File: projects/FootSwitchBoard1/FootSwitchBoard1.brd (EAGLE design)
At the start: 50 x 50 mm, 46 parts

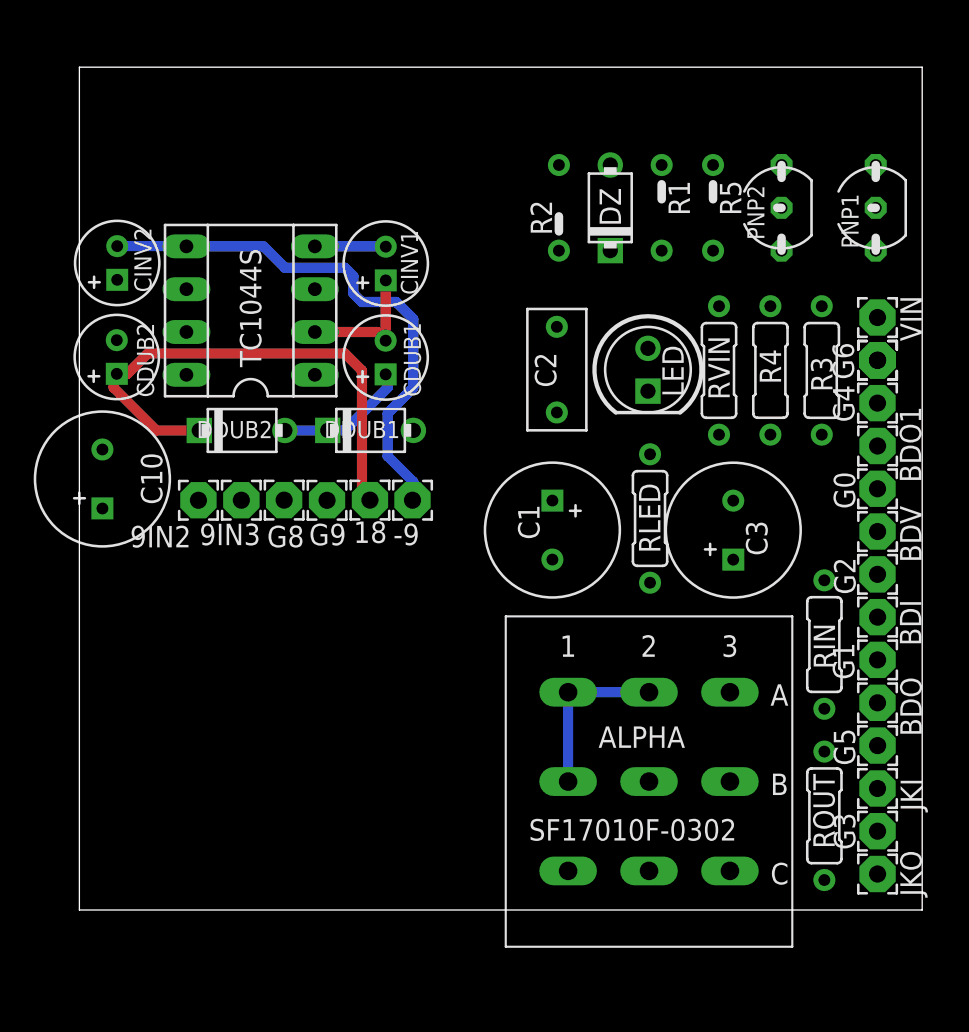
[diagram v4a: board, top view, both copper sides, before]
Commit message: Work in progress, switching back to reverse polarity protection only.
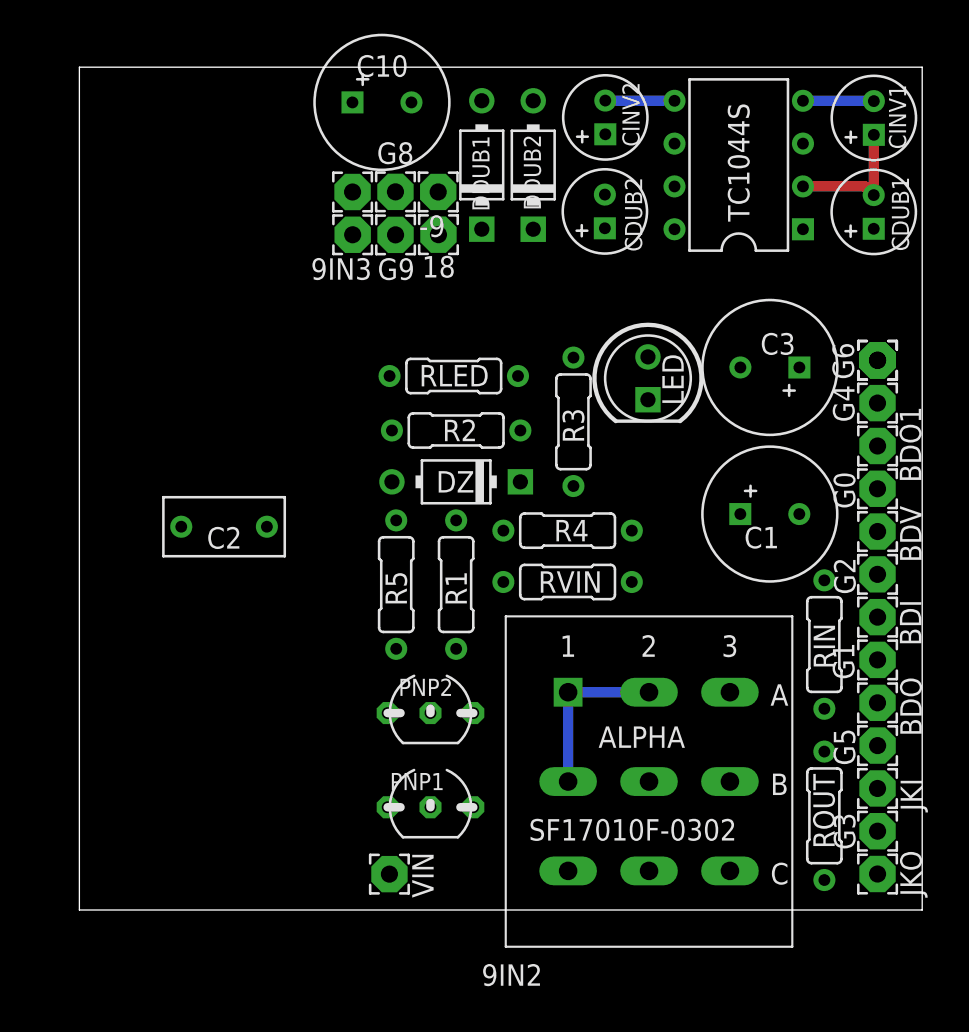
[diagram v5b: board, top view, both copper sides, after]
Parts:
- DDUB1, DDUB2: value 1N58172 -> (none); device gm-diodes:DO41-2 -> gm-diodes:DO41-3
- DZ: device gm-diodes:DO41-2 -> gm-diodes:DO41-3
- R1, R2, R5: device gm-resistors:R0207/2V -> gm-resistors:R0207/3
- TC1044S: device ic-package:SOCKET-08 -> gm-ics:DIL08
- moved PNP1 44.3 mm to (20.8, 6.10), turned to 0 degrees
- moved VIN 43.9 mm to (18.4, 2.13)
- moved PNP2 36.5 mm to (20.8, 11.7), turned to 0 degrees
- moved CDUB2 30.2 mm to (31.2, 41.4)
- moved CINV1 30.2 mm to (47.1, 47.0)
- moved CDUB1 30.2 mm to (47.1, 41.4)
- moved CINV2 30.2 mm to (31.2, 47.0)
- moved TC1044S 30.2 mm to (39.1, 44.2)
- moved R5 29.2 mm to (18.8, 19.3), turned to 90 degrees
- moved C10 27.8 mm to (17.9, 47.9), turned to 0 degrees
- moved R1 25.5 mm to (22.4, 19.3), turned to 90 degrees
- moved DDUB2 23.4 mm to (26.9, 44.2), turned to 90 degrees
- moved C2 21.8 mm to (8.58, 22.7), turned to 180 degrees
- moved 9IN2 20.4 mm to (16.2, 42.6)
- moved G8 19.4 mm to (18.8, 42.6)
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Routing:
- net N$22: track 30.4 -> 0.00 mm
- net N$19: track 32.0 -> 4.11 mm
- net DDUB2: track 7.99 -> 0.00 mm

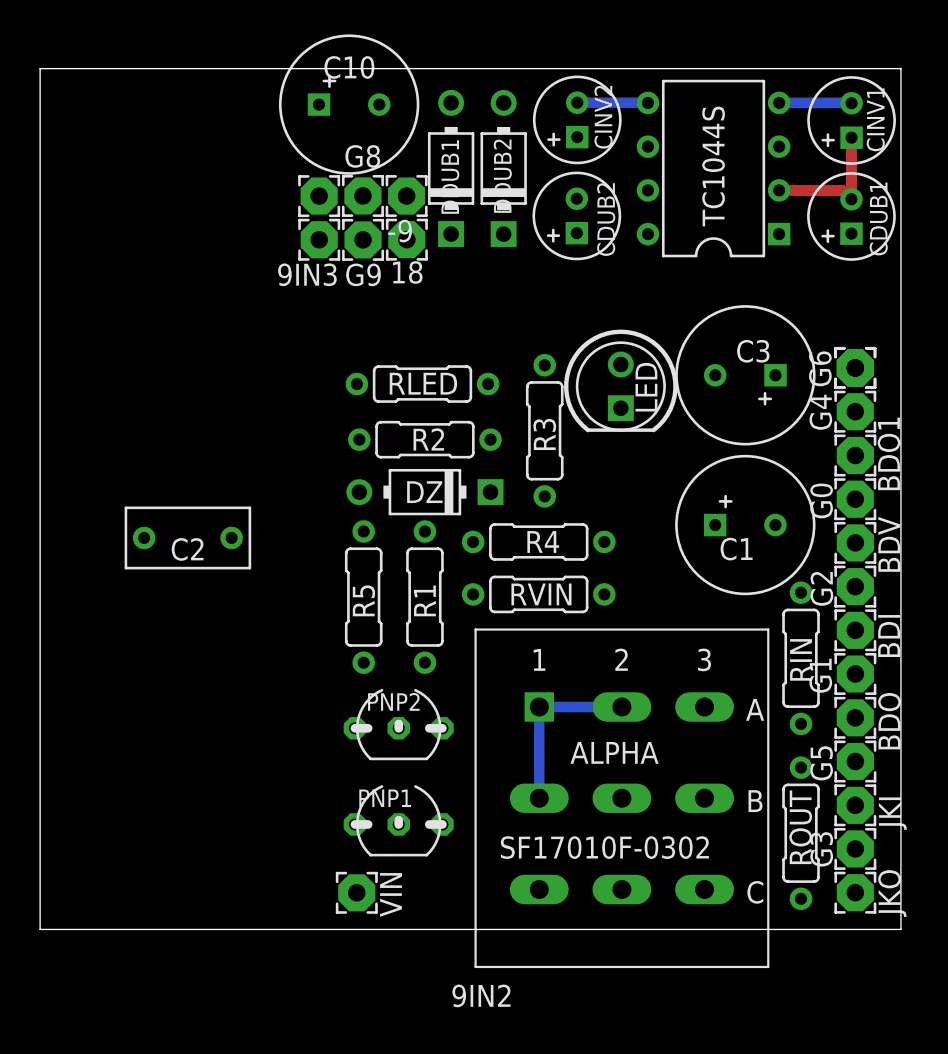
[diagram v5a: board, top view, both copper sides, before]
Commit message: Good layout with reverse polarity protection.
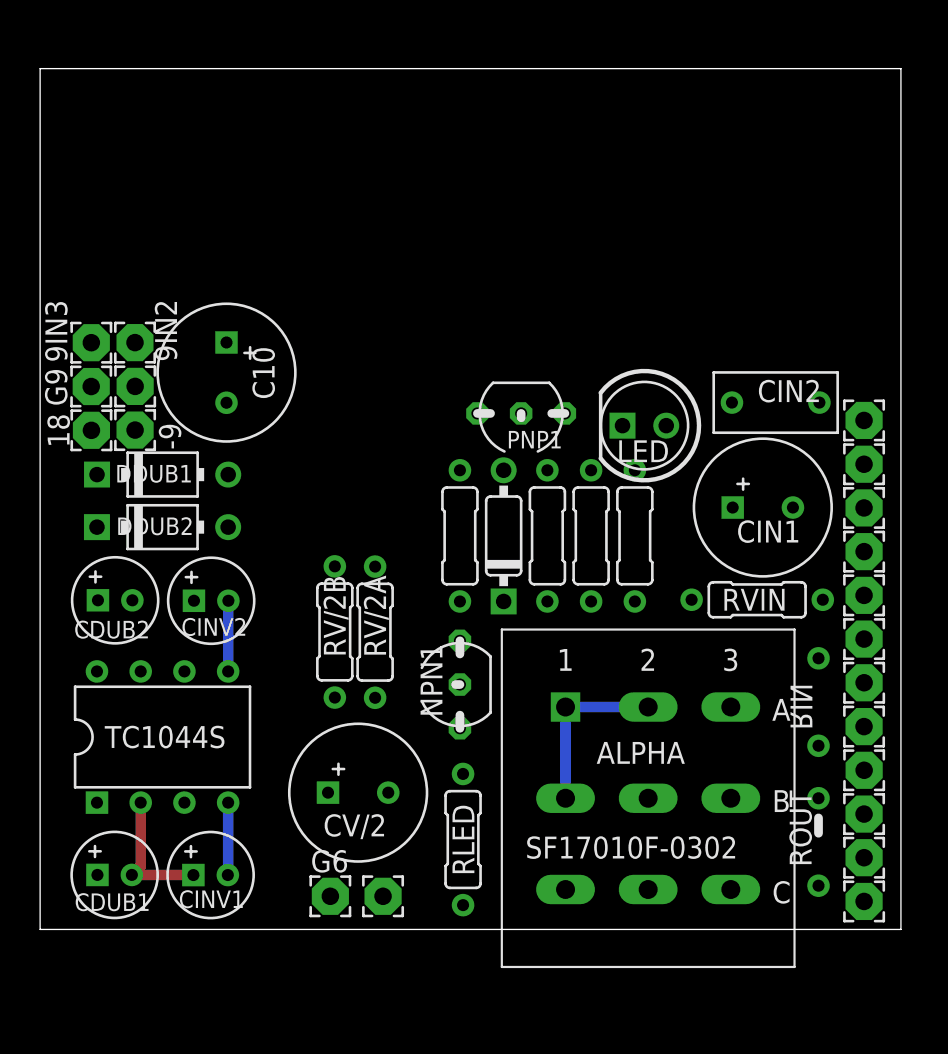
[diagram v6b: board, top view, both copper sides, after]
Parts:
- removed BDO1: WIREPAD2,15/1,0, wirepad:2,15/1,0
- removed C1, C3: 100u, gm-caps-electro-pol:080_035
- removed C2: 100n, gm-caps-film-box:072X035
- removed DZ: (no value), gm-diodes:DO41-3
- removed PNP2: 2N3906-, gm-trans:TO92-
- removed R3, R4: (no value), gm-resistors:R0207/3
- added CIN1, CV/2: 100u, gm-caps-electro-pol:080_035
- added CIN2: 100n, gm-caps-film-box:072X035
- added D1: 1N4148-3, gm-diodes:DO35-3
- added NPN1: 2N3904, gm-trans:TO92-
- added R6: 4M7, gm-resistors:R0207/3
- added RV/2A, RV/2B: (no value), gm-resistors:R0207/3
- R1: value 10k -> 100K
- R2: value 10k -> 3K3
- R5: value 100k -> 10K
- RIN, ROUT: device gm-resistors:R0207/3 -> gm-resistors:R0207/2V
- moved CINV1 57.5 mm to (9.90, 3.16), turned to 0 degrees
- moved CDUB1 57.4 mm to (4.33, 3.17), turned to 0 degrees
- moved TC1044S 46.0 mm to (7.11, 11.2), turned to 0 degrees
- moved G6 43.3 mm to (16.9, 1.93), turned to 0 degrees
- moved V/2 41.2 mm to (19.9, 1.93), turned to 270 degrees
- moved VIN 38.6 mm to (47.9, 27.0)
- moved CINV2 35.1 mm to (9.94, 19.1), turned to 0 degrees
- moved CDUB2 34.9 mm to (4.36, 19.1), turned to 0 degrees
- moved DDUB2 28.7 mm to (7.11, 23.4), turned to 0 degrees
- moved RLED 26.6 mm to (24.6, 5.22), turned to 270 degrees
- moved PNP1 24.9 mm to (27.9, 30.0), turned to 180 degrees
- moved DDUB1 24.4 mm to (7.12, 26.4), turned to 0 degrees
- moved 18 21.4 mm to (2.98, 29.0), turned to 0 degrees
- moved -9 20.8 mm to (5.52, 29.0), turned to 90 degrees
- moved G9 17.9 mm to (2.97, 31.5), turned to 90 degrees
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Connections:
- removed net N$23: PNP1.2, PNP2.1, R1.2
- removed net N$3: BDO.1, BDO1.1, U$1.C3
- removed net N$4: BDI.1, U$1.B2
- new net N$11: BDO.1, ROUT.2, U$1.C3
- new net N$7: PNP1.2, R2.2, R6.1
- new net N$8: BDI.1, RIN.2, U$1.B2
- net 9INDUBINV: now also CIN1.+, CIN2.1; no longer C1.+, C2.1
- net GDUBINV: now also CIN1.-, CIN2.2, CV/2.-, D1.A, NPN1.3, RV/2B.1; no longer C1.-, C2.2, C3.-, DZ.A, R4.1
- net N$1: no longer RIN.2
- net N$10: now also CV/2.+, RV/2A.1, RV/2B.2; no longer C3.+, R3.1, R4.2
- net N$14: now also D1.C, NPN1.2, R1.2; no longer DZ.C, R2.1
- net N$2: no longer ROUT.2
- net N$24: now also R6.2; no longer PNP2.3
- net N$25: now also RV/2A.2; no longer R3.2
- net N$9: now also NPN1.1, R2.1; no longer PNP2.2, R2.2
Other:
- board text removed: "INVERTER BD"

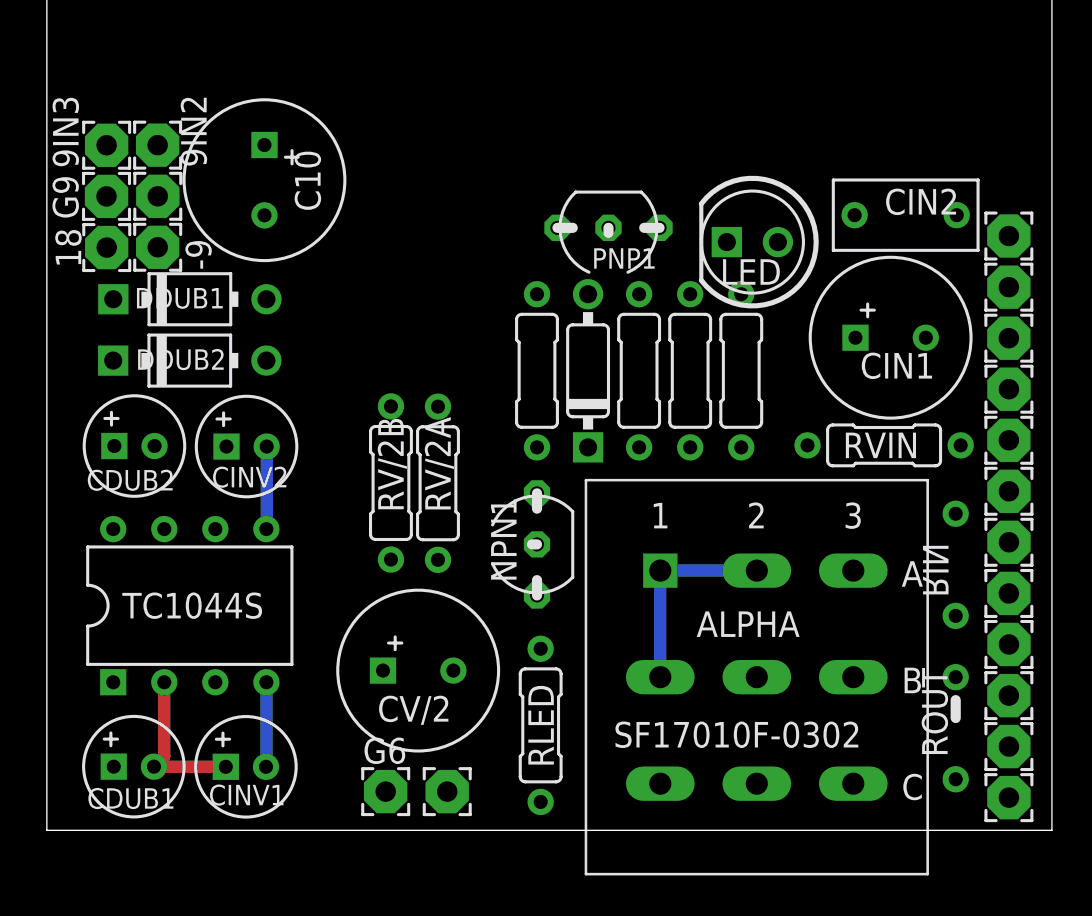
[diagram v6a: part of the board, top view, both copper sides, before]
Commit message: Finalized layout with ground and power planes.
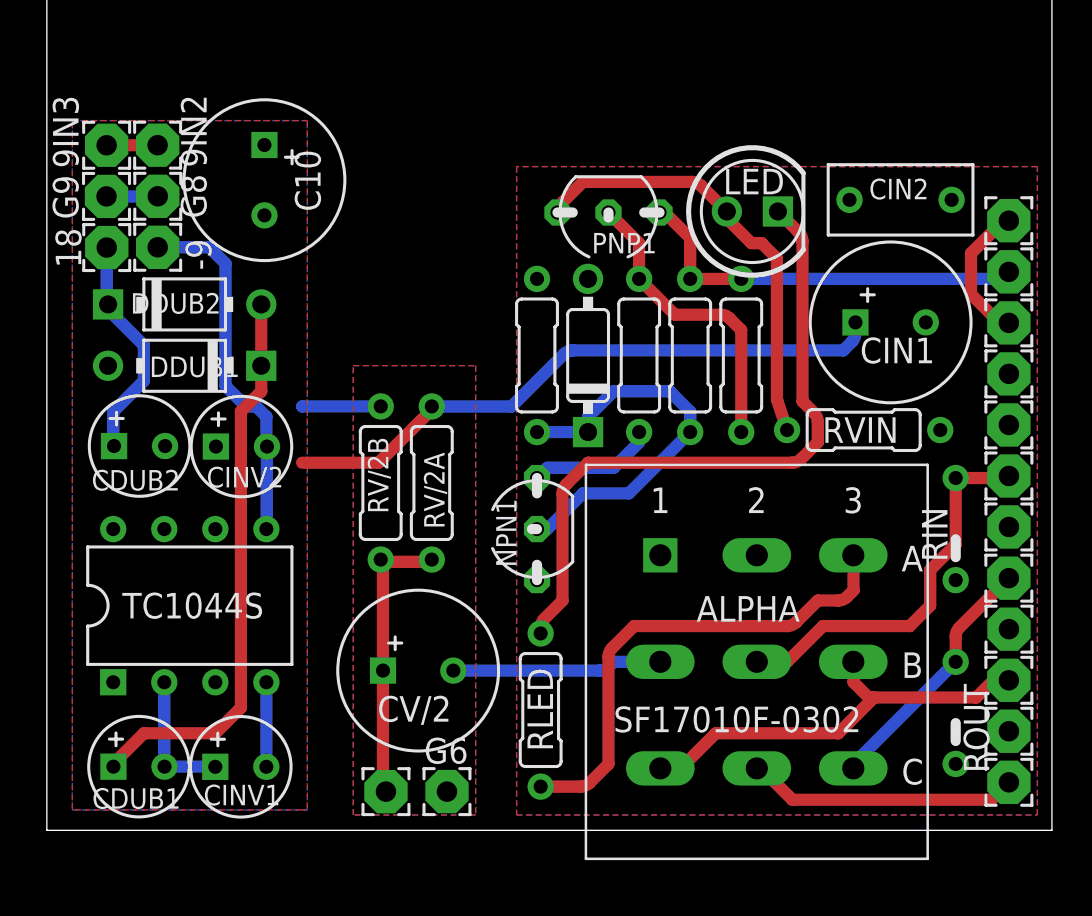
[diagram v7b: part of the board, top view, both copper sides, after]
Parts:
- CDUB1, CDUB2, CINV1, CINV2: device gm-caps-electro-pol:050_020 -> gm-caps-electro-pol:050_020_1
- moved DDUB1 3.32 mm to (6.85, 23.1), turned to 180 degrees
- moved G6 3.05 mm to (19.9, 1.93)
- moved V/2 3.05 mm to (16.9, 1.93)
- moved DDUB2 2.81 mm to (6.86, 26.2)
- moved RIN 1.78 mm to (45.2, 15.0), flipped to the top
- moved LED 1.52 mm to (35.1, 30.8), turned to 0 degrees
- moved RVIN 1.27 mm to (40.6, 19.9)
- moved CIN2 0.80 mm to (42.5, 31.4)
- moved BDO 0.76 mm to (47.9, 12.5)
- moved BDV 0.76 mm to (47.9, 22.7)
- moved CIN1 0.76 mm to (42.0, 25.3)
- moved D1 0.76 mm to (26.9, 23.6)
- moved G0 0.76 mm to (47.9, 25.2)
- moved G1 0.76 mm to (47.9, 15.1)
- moved G2 0.76 mm to (47.9, 20.2)
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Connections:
- removed net N$25: LED.A, PNP1.1, RV/2A.2, RVIN.1
- new net N$4: LED.A, PNP1.1, RVIN.1
- net 9INDUBINV: now also RV/2A.2
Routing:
- net 9INDUBINV: track 0.00 -> 33.4 mm
- net N$5: track 0.00 -> 33.4 mm
- net DDUB2: track 0.00 -> 28.1 mm
- net N$6: track 0.00 -> 24.5 mm
- net N$4: track 0.00 -> 22.0 mm
- net N$1: track 0.00 -> 21.5 mm
- net N$24: track 0.00 -> 20.0 mm
- net N$14: track 0.00 -> 20.0 mm
- net N$8: track 0.00 -> 19.3 mm
- net N$7: track 0.00 -> 15.1 mm
- net N$10: track 0.00 -> 14.1 mm
- net N$19: track 4.11 -> 18.1 mm
- net GDUBINV: track 10.1 -> 24.0 mm
- net N$2: track 0.00 -> 13.5 mm
- net N$11: track 0.00 -> 12.6 mm
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- added copper zone on layer 1, net 9INDUBINV
- added copper zone on layer 16, net GDUBINV

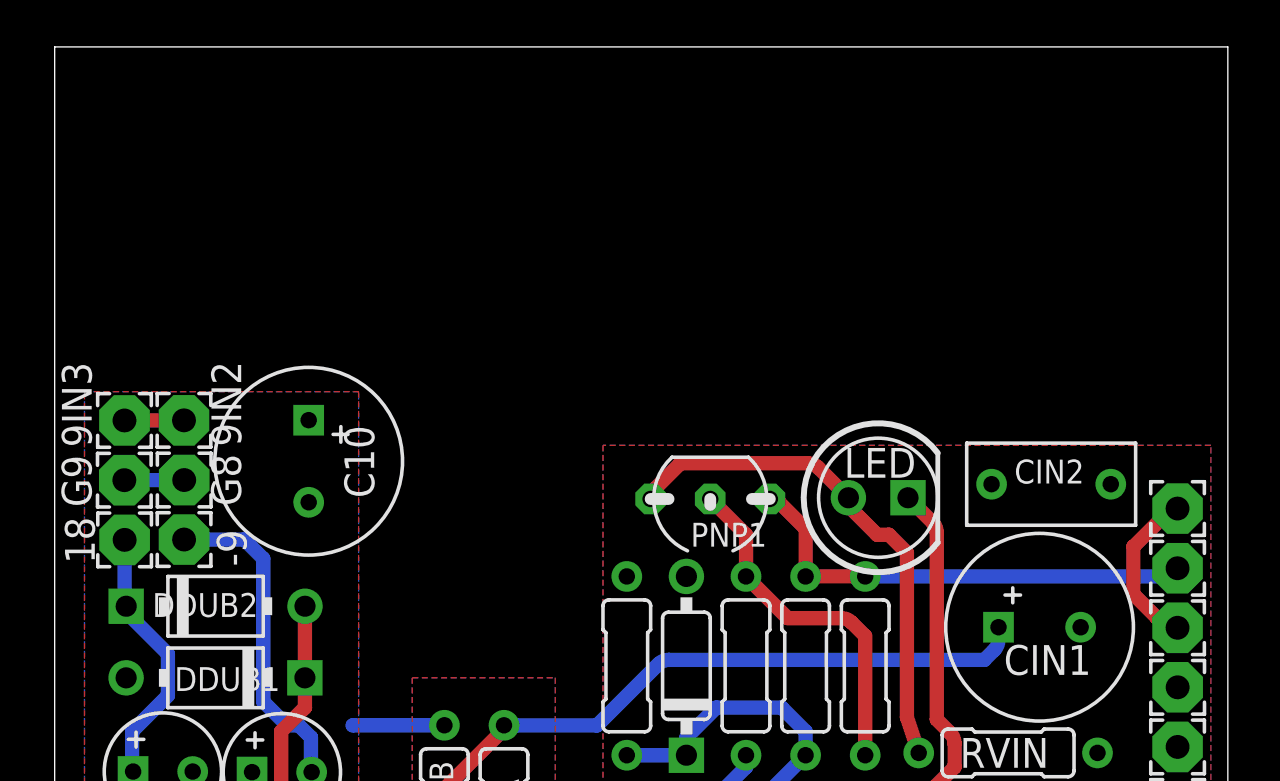
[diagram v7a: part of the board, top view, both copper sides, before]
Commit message: Added prototype area.
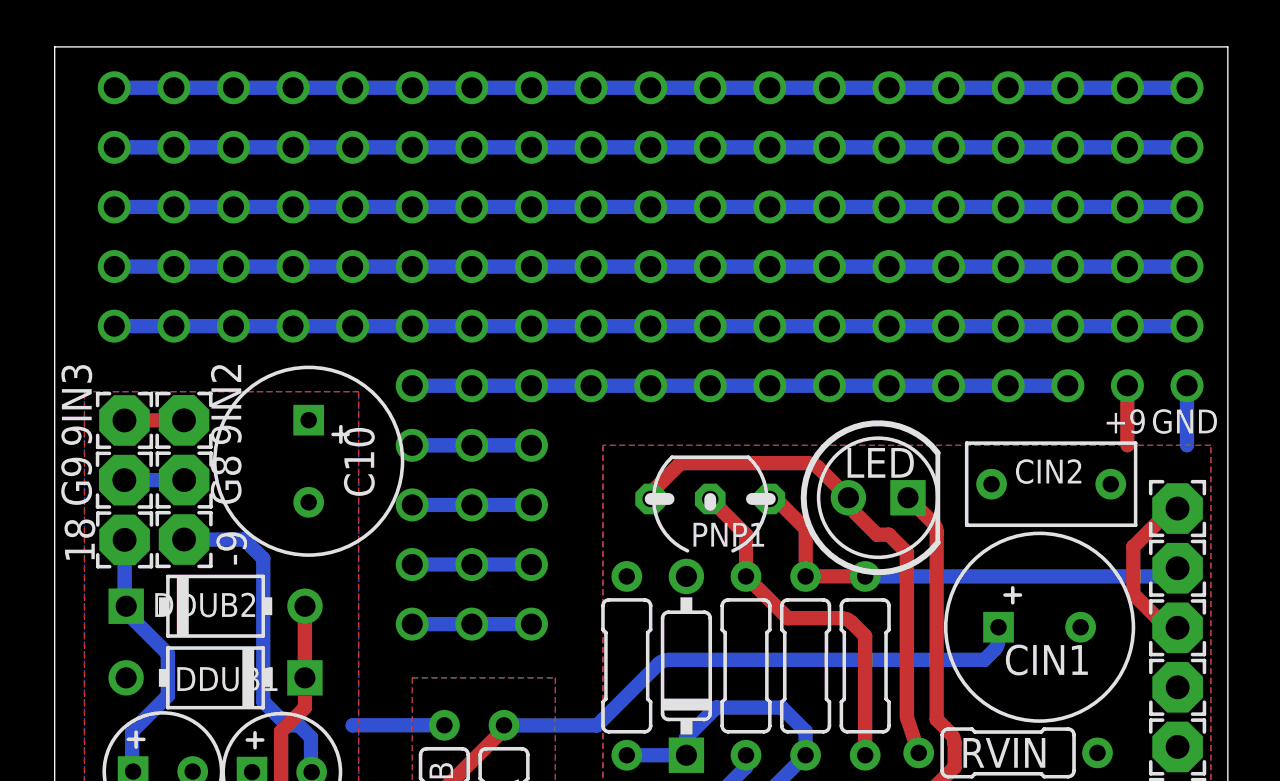
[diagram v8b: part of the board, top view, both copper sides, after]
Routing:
- net N$93: track 0.00 -> 45.7 mm, vias 0 -> 2
- net N$74: track 0.00 -> 45.7 mm, vias 0 -> 2
- net N$55: track 0.00 -> 45.7 mm, vias 0 -> 2
- net N$36: track 0.00 -> 45.7 mm, vias 0 -> 2
- net N$3: track 0.00 -> 45.7 mm, vias 0 -> 2
- net N$125: track 0.00 -> 27.9 mm, vias 0 -> 2
- net N$137: track 0.00 -> 5.08 mm, vias 0 -> 2
- net N$134: track 0.00 -> 5.08 mm, vias 0 -> 2
- net N$131: track 0.00 -> 5.08 mm, vias 0 -> 2
- net N$126: track 0.00 -> 5.08 mm, vias 0 -> 2
- net N$113: track 0.00 -> 2.54 mm, vias 0 -> 1
- net N$112: track 0.00 -> 2.54 mm, vias 0 -> 1
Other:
- board text added: "+9"
- board text added: "GND"
